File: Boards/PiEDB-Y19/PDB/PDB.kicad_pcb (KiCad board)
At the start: 2 copper layers, 112.1 x 88.2 mm, 67 parts, among them J1 Conn_01x02, J2 Conn_01x04, J3 USB_B, Q1 s8050_JSMSEMI, Q2 BSS84, Q3 BSS84, Q4 BSS84, Q5 2N7002, Q6 2N7002, Q7 2N7002, SW2 SW_SPDT, SW3 SW_MEC_5E, Sw1 D-SWITCH_MR5-111-C5N-BB, U2 CH340G, U3 PCF8574, Y1 12MHz

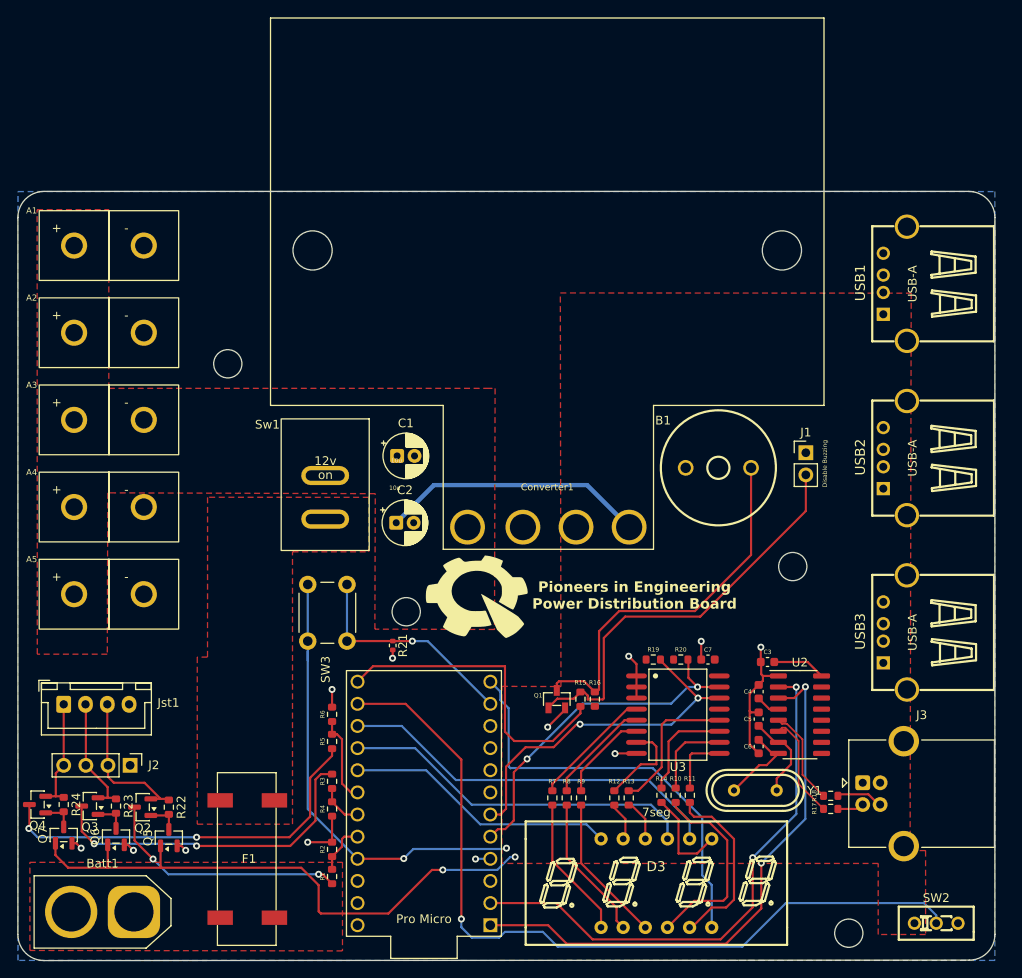
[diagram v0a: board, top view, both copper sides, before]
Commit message: replaced pro micro and CH340G with ATMEGA32U4, added LM66100 power ORing, status LEDs, digit PNP drivers, and USB ESD; INITIAL LAYOUT
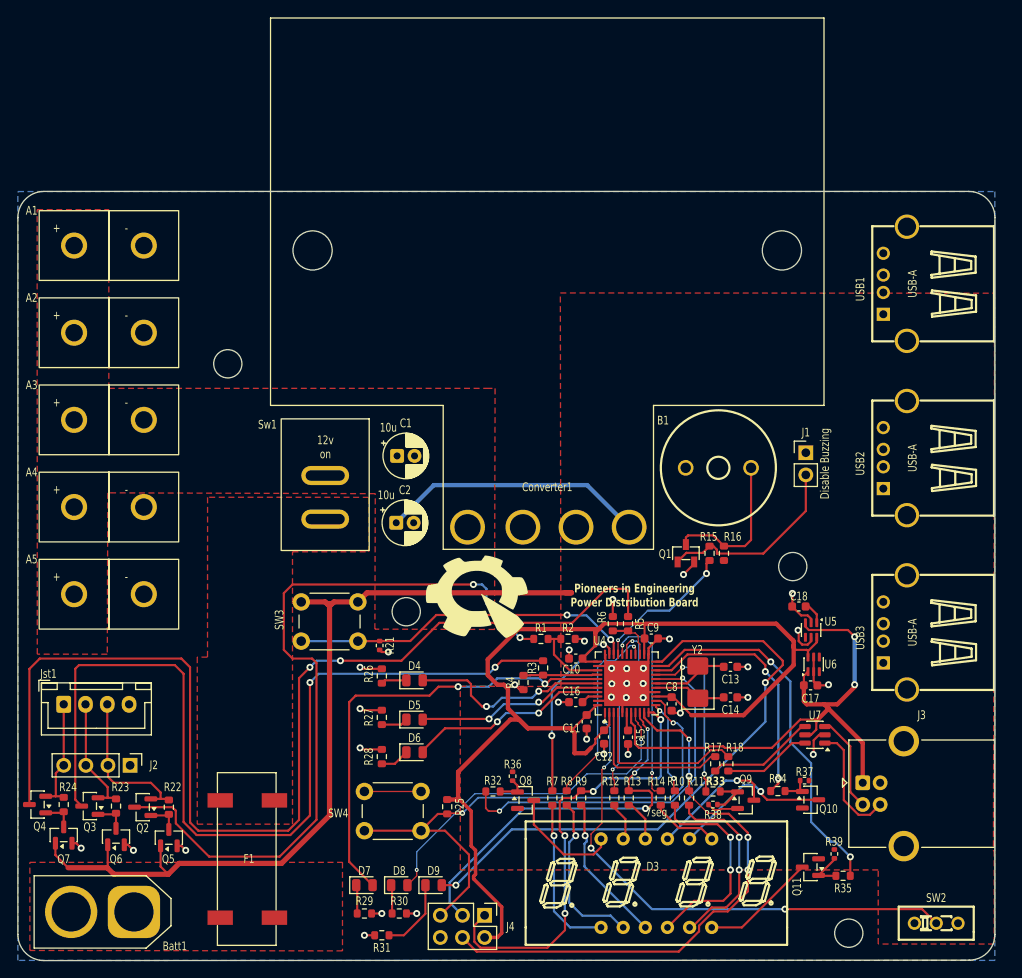
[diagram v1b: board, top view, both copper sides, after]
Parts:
- removed C3, C4: 0.1uF, Capacitor_SMD:C_0603_1608Metric
- removed C5, C6: 22pF, Capacitor_SMD:C_0603_1608Metric
- removed C7: 0.1u, Capacitor_SMD:C_0603_1608Metric
- removed Pro1: ProMicro, PiE_Footprints:ProMicro-EnforcedTop
- removed R19, R20: 4700, Resistor_SMD:R_0603_1608Metric
- removed U2: CH340G, PiE_Footprints:CH340g
- removed U3: PCF8574, PiE_Footprints:PCF8574T
- removed Y1: 12MHz, PiE_Footprints:JYJE S1C12000VWFAC
- added C10: 100nF, Capacitor_SMD:C_0603_1608Metric, F.Cu at (148.8, 102.2)
- added C11: 100nF, Capacitor_SMD:C_0603_1608Metric, F.Cu at (150.0, 109.5)
- added C12: 1uF, Capacitor_SMD:C_0603_1608Metric, F.Cu at (152.0, 111.2)
- added C13: 18pF, Capacitor_SMD:C_0603_1608Metric, F.Cu at (166.5, 103.2)
- added C14: 18pF, Capacitor_SMD:C_0603_1608Metric, F.Cu at (166.5, 106.7)
- added C15: 1uF, Capacitor_SMD:C_0603_1608Metric, F.Cu at (154.8, 111.3)
- added C16: 100nF, Capacitor_SMD:C_0603_1608Metric, F.Cu at (148.8, 107.2)
- added C17: 1uF, Capacitor_SMD:C_0603_1608Metric, F.Cu at (175.7, 105.3)
- added C18: 1uF, Capacitor_SMD:C_0603_1608Metric, F.Cu at (174.3, 96.3)
- added C8: 100nF, Capacitor_SMD:C_0603_1608Metric, F.Cu at (159.8, 107.5)
- added C9: 100nF, Capacitor_SMD:C_0603_1608Metric, F.Cu at (157.4, 100.0)
- added D4: RED, LED_SMD:LED_0805_2012Metric, F.Cu at (130.2, 104.8)
- added D5: YELLOW, LED_SMD:LED_0805_2012Metric, F.Cu at (130.2, 109.2)
- added D6: GREEN, LED_SMD:LED_0805_2012Metric, F.Cu at (130.2, 113.0)
- added D7: RED, LED_SMD:LED_0805_2012Metric, F.Cu at (124.5, 128.2)
- added D8: RED, LED_SMD:LED_0805_2012Metric, F.Cu at (128.5, 128.2)
- added D9: RED, LED_SMD:LED_0805_2012Metric, F.Cu at (132.4, 128.2)
- added J4: AVR-ISP-6, Connector_PinHeader_2.54mm:PinHeader_2x03_P2.54mm_Vertical, F.Cu at (138.3, 131.7)
- added Q10: MMBT3906, Package_TO_SOT_SMD:SOT-23, F.Cu at (175.7, 118.5)
- added Q11: MMBT3906, Package_TO_SOT_SMD:SOT-23, F.Cu at (175.7, 126.2)
- added Q8: MMBT3906, Package_TO_SOT_SMD:SOT-23, F.Cu at (143.0, 118.5)
- added Q9: MMBT3906, Package_TO_SOT_SMD:SOT-23, F.Cu at (168.2, 118.5)
- added R25: 10k, Resistor_SMD:R_0603_1608Metric, F.Cu at (134.0, 119.2)
- added R26: 330, Resistor_SMD:R_0603_1608Metric, F.Cu at (126.5, 104.2)
- added R27: 330, Resistor_SMD:R_0603_1608Metric, F.Cu at (126.5, 109.0)
- added R28: 330, Resistor_SMD:R_0603_1608Metric, F.Cu at (126.5, 113.5)
- added R29: 330, Resistor_SMD:R_0603_1608Metric, F.Cu at (124.5, 131.5)
- added R30: 330, Resistor_SMD:R_0603_1608Metric, F.Cu at (128.5, 131.5)
- added R31: 330, Resistor_SMD:R_0603_1608Metric, F.Cu at (126.5, 134.0)
- added R32: 1k, Resistor_SMD:R_0603_1608Metric, F.Cu at (139.2, 117.5)
- added R33: 1k, Resistor_SMD:R_0603_1608Metric, F.Cu at (164.5, 117.5)
- added R34: 1k, Resistor_SMD:R_0603_1608Metric, F.Cu at (171.9, 117.5)
- added R35: 1k, Resistor_SMD:R_0603_1608Metric, F.Cu at (179.4, 127.2)
- added R36: 10k, Resistor_SMD:R_0402_1005Metric, F.Cu at (141.5, 115.8)
- added R37: 10k, Resistor_SMD:R_0402_1005Metric, F.Cu at (175.0, 116.2)
- added R38: 10k, Resistor_SMD:R_0402_1005Metric, F.Cu at (164.5, 119.0)
- added R39: 10k, Resistor_SMD:R_0402_1005Metric, F.Cu at (178.4, 124.7)
- added SW4: RESET, Button_Switch_THT:SW_PUSH_6mm, F.Cu at (124.5, 117.5)
- added U4: ATmega32U4-M, Package_DFN_QFN:QFN-44-1EP_7x7mm_P0.5mm_EP5.2x5.2mm, F.Cu at (154.6, 105.1)
- added U5: LM66100DCK, Package_TO_SOT_SMD:SOT-363_SC-70-6, F.Cu at (175.8, 99.0)
- added U6: LM66100DCK, Package_TO_SOT_SMD:SOT-363_SC-70-6, F.Cu at (176.0, 102.9)
- added U7: USBLC6-2SC6, Package_TO_SOT_SMD:SOT-23-6, F.Cu at (176.2, 111.0)
- added Y2: 16MHz, Crystal:Crystal_SMD_5032-2Pin_5.0x3.2mm, F.Cu at (162.8, 105.0)
- moved R5 36.6 mm to (154.8, 98.2), turned to 90 degrees
- moved R1 36.3 mm to (144.8, 100.0), turned to 0 degrees
- moved R2 36.3 mm to (147.9, 100.0), turned to 0 degrees
- moved R6 33.8 mm to (153.0, 98.2)
- moved R3 27.5 mm to (145.0, 103.3)
- moved R4 26.3 mm to (142.8, 105.0)
- moved Q1 22.3 mm to (162.3, 92.0)
- moved R16 22.3 mm to (165.8, 90.2)
- moved R15 22.3 mm to (164.1, 90.2)
- moved R17 14.2 mm to (164.8, 114.3), turned to -90 degrees
- moved R18 12.3 mm to (166.2, 114.3), turned to -90 degrees
- moved SW3 4.56 mm to (117.2, 95.8), turned to 0 degrees
- moved R21 1.50 mm to (126.2, 100.8)
- moved R14 0.33 mm to (158.5, 118.2)
- moved R10 0.33 mm to (160.1, 118.2)
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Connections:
- J3 pad 1: unconnected-(J3-VBUS-Pad1) -> /GPIO/USB_VBUS
- R17 pad 1: /USB Data/D- -> /GPIO/USB_D-
- R17 pad 2: Net-(J3-D-) -> Net-(R17-Pad2)
- R18 pad 1: /USB Data/D+ -> /GPIO/USB_D+
- R18 pad 2: Net-(J3-D+) -> Net-(R18-Pad2)
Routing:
- net /GPIO/MCU_5V: track 0.00 -> 139.1 mm
- net /Battery/Cell1+2+3_sw: track 45.3 -> 127.4 mm
- net /GPIO/LED_TX: track 0.00 -> 69.2 mm, vias 0 -> 2
- net /Battery/Cell1+2_sw: track 38.5 -> 105.2 mm
- net /GPIO/RESET: track 0.00 -> 65.3 mm, vias 0 -> 2
- net /Tx: track 64.8 -> 0.00 mm, vias 2 -> 0
- net /GPIO/USB_VBUS: track 0.00 -> 64.4 mm, vias 0 -> 2
- net /Rx: track 62.7 -> 0.00 mm, vias 2 -> 0
- net /Battery/Cell1_sw: track 28.5 -> 87.4 mm
- net /GPIO/G: track 7.22 -> 65.1 mm, vias 0 -> 4
- net /GPIO/LED_HEARTBEAT: track 0.00 -> 52.4 mm, vias 0 -> 2
- net /GPIO/DIG4_N: track 0.00 -> 43.1 mm, vias 0 -> 2
- net /GPIO/DIG1_N: track 0.00 -> 42.9 mm, vias 0 -> 2
- net /GPIO/SCL: track 40.8 -> 0.00 mm, vias 2 -> 0
- net /GPIO/DP: track 10.5 -> 51.1 mm, vias 0 -> 4
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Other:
- board text removed: "Pro Micro"

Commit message: rerouted PDB to final satisfaction; need to add testpoints
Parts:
- added C19: 1uF, Capacitor_SMD:C_0603_1608Metric, F.Cu at (177.2, 105.4)
- J3: footprint Connector_USB:USB_B_OST_USB-B1HSxx_Horizontal -> PiE_Footprints:USB_B_OST_USB-B1HSxx_Horizontal
- U4: footprint Package_DFN_QFN:QFN-44-1EP_7x7mm_P0.5mm_EP5.2x5.2mm -> PiE_Footprints:QFN-44-1EP_7x7mm_P0.5mm_EP5.2x5.2mm
- moved J4 47.5 mm to (169.0, 95.5), turned to 0 degrees
- moved R35 42.0 mm to (142.5, 107.2), turned to -90 degrees
- moved R39 41.8 mm to (140.0, 108.2), turned to 180 degrees
- moved Q11 37.4 mm to (141.5, 111.0), turned to -90 degrees
- moved R25 36.6 mm to (165.2, 100.2)
- moved C13 15.5 mm to (152.0, 97.8), turned to 90 degrees
- moved R6 13.1 mm to (149.2, 110.8), turned to 180 degrees
- moved R5 12.1 mm to (149.2, 109.0), turned to 180 degrees
- moved C10 11.2 mm to (153.3, 112.5), turned to -90 degrees
- moved C16 10.9 mm to (158.3, 112.5), turned to -90 degrees
- moved C11 10.7 mm to (160.6, 111.2), turned to 0 degrees
- moved R31 10.6 mm to (132.5, 125.2), turned to 0 degrees
- moved C12 10.5 mm to (162.3, 109.2), turned to 0 degrees
- moved C14 10.3 mm to (160.2, 98.5), turned to 90 degrees
- moved Y2 9.37 mm to (156.0, 98.5), turned to 180 degrees
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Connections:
- J4 pad 1: /GPIO/DP -> /GPIO/BatCal
- J4 pad 3: /GPIO/F -> /GPIO/ISP_SCK
- J4 pad 4: /GPIO/G -> /Buzzer
- U4 pad 1: /GPIO/toggle -> /GPIO/DIG3_N
- U4 pad 10: /GPIO/G -> /Buzzer
- U4 pad 11: /GPIO/DP -> /GPIO/BatCal
- U4 pad 12: /GPIO/C -> /GPIO/toggle
- U4 pad 18: /GPIO/DIG1_N -> /GPIO/LED_RED
- U4 pad 19: /GPIO/DIG2_N -> /GPIO/LED_YELLOW
- U4 pad 20: /GPIO/DIG3_N -> /GPIO/LED_GREEN
- U4 pad 21: /GPIO/DIG4_N -> /GPIO/LED_HEARTBEAT
- U4 pad 25: /Cell1+2+3_s -> /Cell1_s
- U4 pad 26: /GPIO/D -> /Cell1+2_s
- U4 pad 27: unconnected-(U4-PD7-Pad27) -> /Cell1+2+3_s
- U4 pad 28: /GPIO/A -> /GPIO/DIG4_N
- U4 pad 29: /GPIO/B -> /GPIO/DIG1_N
- U4 pad 30: /Buzzer -> /GPIO/E
- U4 pad 31: /GPIO/BatCal -> /GPIO/D
- U4 pad 32: /GPIO/E -> /GPIO/DP
- U4 pad 36: /Cell1_s -> /GPIO/A
- U4 pad 37: /Cell1+2_s -> /GPIO/F
- U4 pad 38: /GPIO/LED_HEARTBEAT -> /GPIO/B
- U4 pad 39: /GPIO/LED_RED -> /GPIO/C
- U4 pad 40: /GPIO/LED_YELLOW -> /GPIO/G
- U4 pad 41: /GPIO/LED_GREEN -> /GPIO/DIG2_N
- U4 pad 9: /GPIO/F -> /GPIO/ISP_SCK
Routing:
- net /GPIO/G: track 65.1 -> 9.82 mm, vias 4 -> 2
- net /GPIO/LED_RX: track 40.0 -> 90.5 mm, vias 2 -> 4
- net /GPIO/DP: track 51.1 -> 10.6 mm, vias 4 -> 2
- net /GPIO/F: track 45.6 -> 7.86 mm, vias 3 -> 2
- net /GPIO/Dig4: track 13.3 -> 49.3 mm, vias 0 -> 2
- net /GPIO/DIG4_N: track 43.1 -> 10.7 mm
- net /GPIO/BatCal: track 39.8 -> 68.5 mm
- net /GPIO/DIG1_N: track 42.9 -> 15.6 mm
- net /GPIO/RESET: track 65.3 -> 92.4 mm, vias 2 -> 4
- net /GPIO/LED_TX: track 69.2 -> 50.7 mm, vias 2 -> 4
- net /Battery/Cell1_sw: track 87.4 -> 71.8 mm, vias 2 -> 4
- net /GPIO/USB_VBUS: track 64.4 -> 49.8 mm, vias 2 -> 0
- net /GPIO/LED_GREEN: track 23.1 -> 37.7 mm, vias 2 -> 4
- net /GPIO/ISP_SCK: track 0.00 -> 14.5 mm, vias 0 -> 1
- net /GPIO/B: track 22.9 -> 8.67 mm
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
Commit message: fixed USB-B 3d model
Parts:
- Converter1: value 5v_converter -> BUCK_CONVERTER_5V

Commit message: added test points to board and revA silkscreen, as well as general silkscreen text that will help board readability
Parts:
- added 5V1: TestPoint, TestPoint:TestPoint_Loop_D2.60mm_Drill0.9mm_Beaded, F.Cu at (180.5, 69.0)
- added GND1: TestPoint, TestPoint:TestPoint_Loop_D2.60mm_Drill0.9mm_Beaded, F.Cu at (181.2, 89.0)
- added MCU_5V1: TestPoint, TestPoint:TestPoint_Loop_D2.60mm_Drill0.9mm_Beaded, F.Cu at (136.8, 106.8)
- added USB_VBUS1: TestPoint, TestPoint:TestPoint_Loop_D2.60mm_Drill0.9mm_Beaded, F.Cu at (177.8, 94.2)
- Converter1: value BUCK_CONVERTER_5V -> 5v_converter
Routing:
- net /GPIO/MCU_5V: track 127.0 -> 136.7 mm
- net /GPIO/USB_VBUS: track 49.8 -> 54.3 mm
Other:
- board text added: "BATTERY STATUS"
- board text added: "Change Network"
- board text added: "ISP"
- board text added: "RevA PiEDB-Y19 G. Lopez 10/1/2026"
